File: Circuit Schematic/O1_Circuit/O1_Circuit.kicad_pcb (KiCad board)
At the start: 2 copper layers, 17 parts, among them J1 Screw_Terminal_Battery, J2 GP2Y0A21YK0F_Sensor1, J3 GP2Y0A21YK0F_Sensor2, J4 TM4C1294XL Used Pin, M1 Motor_DC, M2 Motor_DC, Q1 TIP120, Q2 TIP120, U3 L7805

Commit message: Fiishing PCB
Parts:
- J1: value Screw_Terminal_Battery -> Screw Terminal Battery
- Motor 1: renamed from M1
- Sensor 2: renamed from J2
- moved R3 82.8 mm to (117.0, 105.0), turned to 180 degrees
- moved M2 74.7 mm to (106.0, 89.5), turned to 180 degrees
- moved R2 71.4 mm to (129.0, 105.0), turned to 180 degrees
- moved J3 65.3 mm to (116.1, 123.0), turned to 180 degrees
- moved R1 61.5 mm to (140.0, 105.0)
- moved C1 53.7 mm to (126.0, 70.0), turned to 180 degrees
- moved L7805 50.9 mm to (136.5, 69.9)
- moved R4 48.3 mm to (151.2, 105.0)
- moved C2 48.3 mm to (126.0, 79.0), turned to 180 degrees
- moved Q1 46.0 mm to (151.9, 114.0)
- moved D2 44.6 mm to (149.7, 90.2)
- moved J1 40.1 mm to (121.9, 55.8), turned to 180 degrees
- moved Sensor 2 35.6 mm to (152.9, 124.0)
- moved Motor 1 26.2 mm to (163.5, 90.0), turned to 180 degrees
- moved D1 24.5 mm to (118.0, 89.5), turned to 180 degrees
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- renumbered U3 to L7805
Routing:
- net +7.5V: track 0.00 -> 153.5 mm
- net +5V: track 0.00 -> 105.1 mm
- net Net-(D1-A): track 0.00 -> 35.0 mm
- net /PE2: track 0.00 -> 34.0 mm
- net Net-(D2-A): track 0.00 -> 33.5 mm
- net /PE3: track 0.00 -> 30.8 mm
- net Net-(Q1-B): track 0.00 -> 13.6 mm
- net Net-(Q2-B): track 0.00 -> 11.8 mm
- net /PA5: track 0.00 -> 4.84 mm
- net /PA4: track 0.00 -> 4.38 mm
- added copper zone on F.Cu, net GND
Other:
- board outline added: 71 x 100 mm

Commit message: Touch up PCB
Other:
- board size 71 x 100 mm -> 70 x 83 mm
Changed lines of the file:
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@@
 	(gr_rect
 		(start 98.5 49)
-		(end 169.5 149)
+		(end 168.5 132)
 		(stroke
 			(width 0.05)
@@
 		(polygon
 			(pts
-				(xy 170 49) (xy 98 49) (xy 98 150) (xy 170 150)
+				(xy 169 49) (xy 98 49) (xy 98 133) (xy 169 133)
 			)
 		)

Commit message: PCB Design Edit
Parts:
- added H1: MountingHole, MountingHole:MountingHole_2.5mm, F.Cu at (164.0, 53.0)
- added H2: MountingHole, MountingHole:MountingHole_2.5mm, F.Cu at (103.0, 53.0)
- added H3: MountingHole, MountingHole:MountingHole_2.5mm, F.Cu at (165.0, 128.0)
- added H4: MountingHole, MountingHole:MountingHole_2.5mm, F.Cu at (103.0, 128.0)
- J1: value Screw Terminal Battery -> Screw_Terminal_Battery
- J2: renamed from Sensor 2
- M1: renamed from Motor 1
- renumbered L7805 to U3

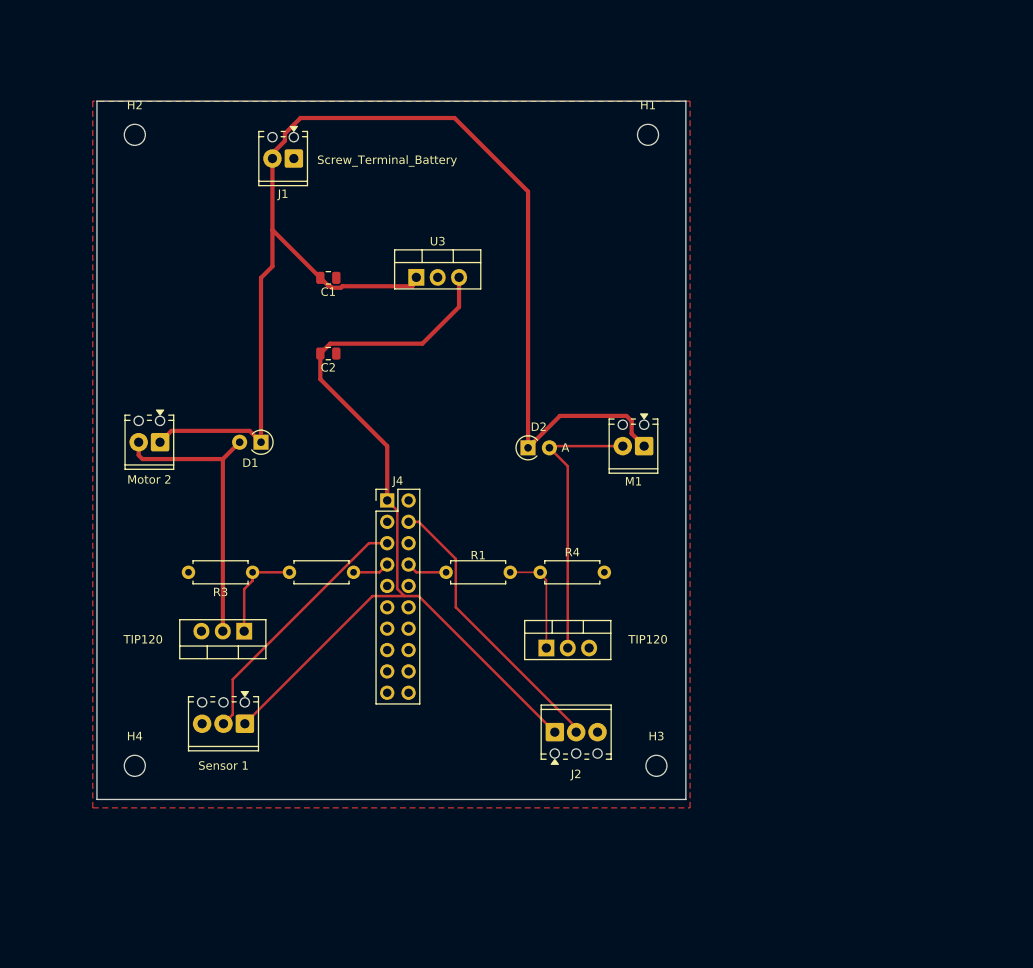
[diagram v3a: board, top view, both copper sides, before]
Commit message: Editing PCB due to short on prev
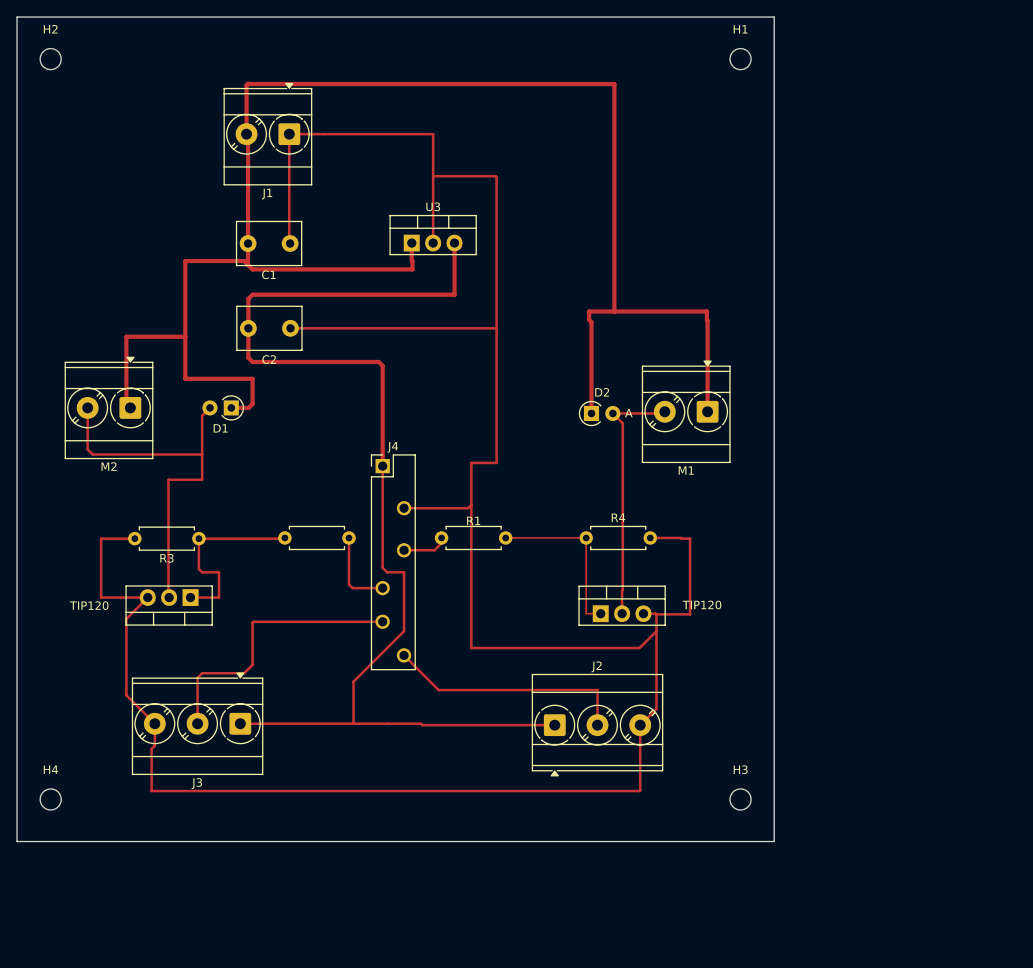
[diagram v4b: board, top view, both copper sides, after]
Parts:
- C1, C2: footprint Capacitor_SMD:C_0805_2012Metric -> Capacitor_THT:C_Disc_D7.5mm_W5.0mm_P5.00mm
- J1, M1, M2: footprint TerminalBlock_Phoenix:TerminalBlock_Phoenix_MPT-0,5-2-2.54_1x02_P2.54mm_Horizontal -> TerminalBlock_Phoenix:TerminalBlock_Phoenix_MKDS-3-2-5.08_1x02_P5.08mm_Horizontal
- J2, J3: footprint TerminalBlock_Phoenix:TerminalBlock_Phoenix_MPT-0,5-3-2.54_1x03_P2.54mm_Horizontal -> TerminalBlock_Phoenix:TerminalBlock_Phoenix_MKDS-3-3-5.08_1x03_P5.08mm_Horizontal
- moved H1 14.2 mm to (175.0, 44.0)
- moved H2 13.5 mm to (93.0, 44.0)
- moved H3 10.8 mm to (175.0, 132.0)
- moved H4 10.8 mm to (93.0, 132.0)
- moved M1 8.57 mm to (171.1, 85.9)
- moved D2 8.57 mm to (157.3, 86.1)
- moved Q1 7.64 mm to (158.4, 109.9)
- moved Q2 7.53 mm to (109.6, 108.0)
- moved R3 7.53 mm to (110.6, 101.0)
- moved R4 6.82 mm to (156.7, 100.9)
- moved C1 6.10 mm to (121.5, 65.9)
- moved C2 5.41 mm to (121.5, 76.0)
- moved D1 5.39 mm to (114.5, 85.5)
- moved M2 5.39 mm to (102.5, 85.5)
- moved U3 4.12 mm to (135.9, 65.9)
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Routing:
- net GND: track 0.00 -> 307.6 mm
- net +7.5V: track 153.5 -> 207.8 mm
- net +5V: track 105.1 -> 138.9 mm
- net Net-(Q2-B): track 11.8 -> 22.8 mm
- net Net-(D1-A): track 35.0 -> 45.8 mm
- net Net-(Q1-B): track 13.6 -> 20.7 mm
- net /PA4: track 4.38 -> 9.71 mm
- net /PE2: track 34.0 -> 28.9 mm
- net /PE3: track 30.8 -> 33.1 mm
- net Net-(D2-A): track 33.5 -> 31.4 mm
- net /PA5: track 4.84 -> 5.43 mm
- removed copper zone on F.Cu, net GND
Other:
- board size 70 x 83 mm -> 90 x 98 mm

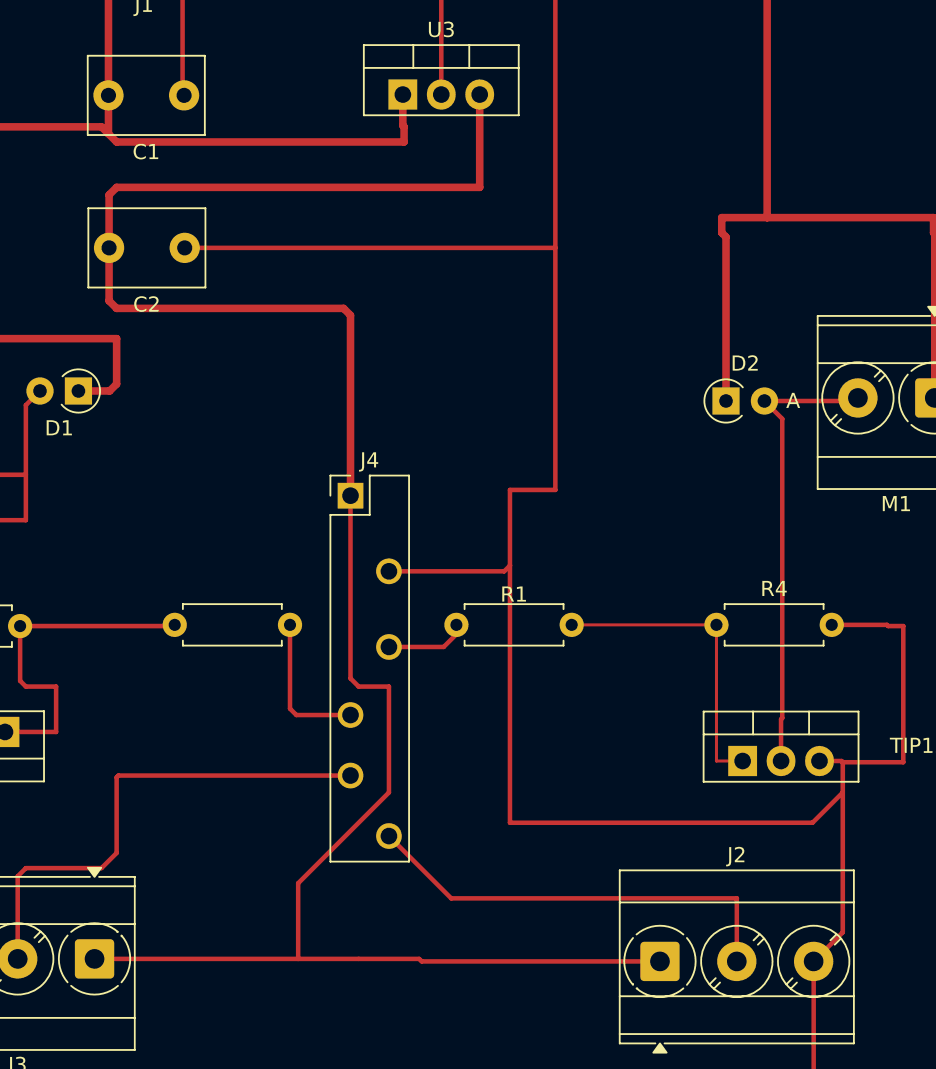
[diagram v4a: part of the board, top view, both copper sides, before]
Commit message: Calibrating Distance Sensor Obstacle Detection
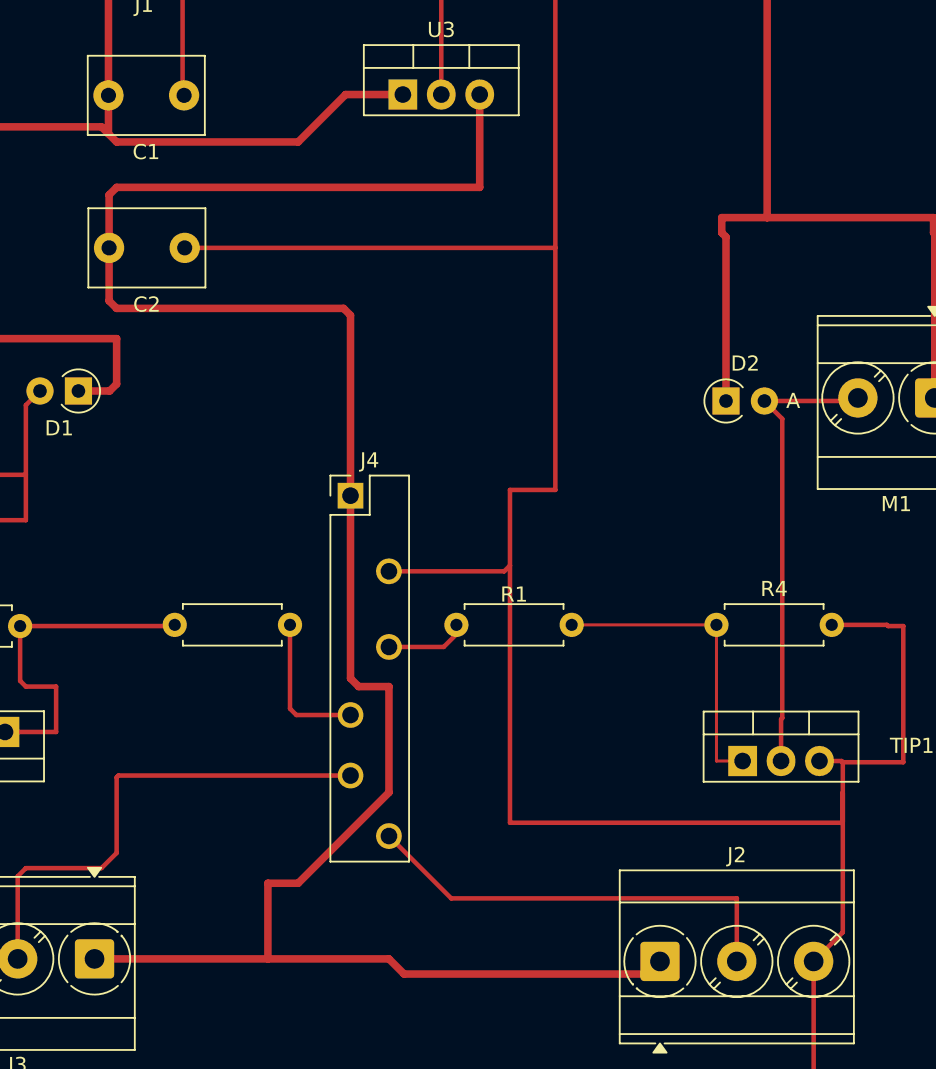
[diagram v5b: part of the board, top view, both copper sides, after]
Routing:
- net +5V: track 138.9 -> 141.6 mm
- net +7.5V: track 207.8 -> 205.9 mm
- net GND: track 307.6 -> 308.7 mm
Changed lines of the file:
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@@
 			(drillshape 0)
 			(scaleselection 1)
-			(outputdirectory "Gerber/")
+			(outputdirectory "Gerber And Drill/")
 		)
 	)
@@
 	)
 	(segment
+		(start 143 114)
+		(end 165 114)
+		(width 0.3)
+		(layer "F.Cu")
+		(net 1)
+	)
+	(segment
 		(start 169 110)
 		(end 169 101)
@@
 	)
 	(segment
+		(start 165 114)
+		(end 165 112)
+		(width 0.3)
+		(layer "F.Cu")
+		(net 1)
+	)
+	(segment
 		(start 163.075 130.925)
 		(end 163 131)
@@
 	)
 	(segment
-		(start 143 114)
-		(end 163 114)
-		(width 0.3)
-		(layer "F.Cu")
-		(net 1)
-	)
-	(segment
 		(start 135 97.38)
 		(end 142.62 97.38)
@@
 	)
 	(segment
-		(start 163 114)
-		(end 165 112)
-		(width 0.3)
-		(layer "F.Cu")
-		(net 1)
-	)
-	(segment
 		(start 164.92 109.92)
 		(end 163.46 109.92)
@@
 	)
 	(segment
-		(start 117 69)
-		(end 136 69)
-		(width 0.5)
-		(layer "F.Cu")
-		(net 2)
-	)
-	(segment
 		(start 109 77)
 		(end 102 77)
@@
 	)
 	(segment
+		(start 129 69)
+		(end 132.135 65.865)
+		(width 0.5)
+		(layer "F.Cu")
+		(net 2)
+	)
+	(segment
 		(start 114.4745 85.46)
 		(end 114.0145 85.46)
@@
 	)
 	(segment
-		(start 136 68)
-		(end 135.92 67.92)
+		(start 117 69)
+		(end 129 69)
 		(width 0.5)
 		(layer "F.Cu")
@@
 	)
 	(segment
-		(start 135.92 67.92)
-		(end 135.92 65.865)
-		(width 0.5)
-		(layer "F.Cu")
-		(net 2)
-	)
-	(segment
 		(start 160 74)
 		(end 171 74)
@@
 	)
 	(segment
-		(start 116.46 68.46)
-		(end 117 69)
+		(start 109 82)
+		(end 117 82)
 		(width 0.5)
 		(layer "F.Cu")
@@
 	)
 	(segment
-		(start 109 82)
-		(end 117 82)
+		(start 109 77)
+		(end 109 82)
 		(width 0.5)
 		(layer "F.Cu")
@@
 	)
 	(segment
-		(start 109 77)
-		(end 109 82)
+		(start 132.135 65.865)
+		(end 135.92 65.865)
 		(width 0.5)
 		(layer "F.Cu")
@@
 	)
 	(segment
-		(start 116.54 85.46)
-		(end 114.4745 85.46)
+		(start 116.46 68.46)
+		(end 117 69)
 		(width 0.5)
 		(layer "F.Cu")
@@
 	)
 	(segment
-		(start 136 69)
-		(end 136 68)
+		(start 116.54 85.46)
+		(end 114.4745 85.46)
 		(width 0.5)
 		(layer "F.Cu")
@@
 	)
 	(segment
-		(start 115.54 123)
-		(end 129 123)
-		(width 0.3)
+		(start 152.0825 124)
+		(end 152.915 123.1675)
+		(width 0.5)
 		(layer "F.Cu")
 		(net 3)
 	)
 	(segment
-		(start 129 123)
-		(end 133 123)
-		(width 0.3)
+		(start 135 123)
+		(end 136 124)
+		(width 0.5)
 		(layer "F.Cu")
 		(net 3)
 	)
 	(segment
-		(start 137 123)
-		(end 137.1675 123.1675)
-		(width 0.3)
+		(start 127 123)
+		(end 127 118)
+		(width 0.5)
 		(layer "F.Cu")
 		(net 3)
@@
 	)
 	(segment
-		(start 135 112)
-		(end 135 105)
-		(width 0.3)
+		(start 127 118)
+		(end 129 118)
+		(width 0.5)
+		(layer "F.Cu")
+		(net 3)
+	)
+	(segment
+		(start 127 123)
+		(end 135 123)
+		(width 0.5)
 		(layer "F.Cu")
 		(net 3)
@@
 		(start 133 105)
 		(end 132.46 104.46)
-		(width 0.3)
+		(width 0.5)
 		(layer "F.Cu")
 		(net 3)
@@
 	)
 	(segment
-		(start 129 118)
-		(end 135 112)
-		(width 0.3)
-		(layer "F.Cu")
-		(net 3)
-	)
-	(segment
-		(start 132.46 104.46)
-		(end 132.46 92.38)
-		(width 0.3)
-		(layer "F.Cu")
-		(net 3)
-	)
-	(segment
 		(start 141 72)
 		(end 117 72)
@@
 	)
 	(segment
-		(start 116.5 79.5)
-		(end 117 80)
+		(start 129 118)
+		(end 135 112)
 		(width 0.5)
 		(layer "F.Cu")
@@
 	)
 	(segment
-		(start 137.1675 123.1675)
-		(end 152.915 123.1675)
-		(width 0.3)
+		(start 116.5 79.5)
+		(end 117 80)
+		(width 0.5)
 		(layer "F.Cu")
 		(net 3)
 	)
 	(segment
-		(start 133 123)
-		(end 137 123)
-		(width 0.3)
+		(start 132.46 104.46)
+		(end 132.46 92.38)
+		(width 0.5)
 		(layer "F.Cu")
 		(net 3)
@@
 		(start 135 105)
 		(end 133 105)
-		(width 0.3)
+		(width 0.5)
 		(layer "F.Cu")
 		(net 3)
 	)
 	(segment
-		(start 129 123)
-		(end 129 118)
-		(width 0.3)
+		(start 135 112)
+		(end 135 105)
+		(width 0.5)
+		(layer "F.Cu")
+		(net 3)
+	)
+	(segment
+		(start 115.54 123)
+		(end 127 123)
+		(width 0.5)
+		(layer "F.Cu")
+		(net 3)
+	)
+	(segment
+		(start 136 124)
+		(end 152.0825 124)
+		(width 0.5)
 		(layer "F.Cu")
 		(net 3)
